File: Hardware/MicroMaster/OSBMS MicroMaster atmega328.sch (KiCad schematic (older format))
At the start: 8 parts

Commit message: changing resistor design
changing resistor design to be cheaper to make and put out a more
manageable amount of heat.
previous design archived
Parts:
- removed U?: PHOTORESISTOR, symbol PHOTORESISTOR
- added Q? (x2): FDS6892A, SO8, symbol FDS6892A
- added R?: 100 ohm, symbol R
- added R?: 4.7k, symbol R
- added U? (x2): optoisolator, symbol optoisolator
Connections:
- net labels added: +3.3V, CLK, CS_N, GND, IRQ, MISO, MOSI, PD-N, RST, RXI, SCK, TXO
- wire segments 0 -> 31
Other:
- moved on the sheet: P?
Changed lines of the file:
@@
 LIBS:contrib
 LIBS:valves
+LIBS:Open source BMS
+LIBS:ata6870n_bms
 LIBS:OSBMS MicroMaster atmega328-cache
 EELAYER 25 0
@@
 L CONN_01X09 P?
 U 1 1 5434A7AE
-P 9450 1150
-F 0 "P?" H 9450 1650 50  0000 C CNN
-F 1 "CONN_01X09" V 9550 1150 50  0000 C CNN
-F 2 "" H 9450 1150 60  0000 C CNN
-F 3 "" H 9450 1150 60  0000 C CNN
-	1    9450 1150
-	0    -1   -1   0
+P 10850 2150
+F 0 "P?" H 10850 2650 50  0000 C CNN
+F 1 "CONN_01X09" V 10950 2150 50  0000 C CNN
+F 2 "" H 10850 2150 60  0000 C CNN
+F 3 "" H 10850 2150 60  0000 C CNN
+	1    10850 2150
+	1    0    0    -1
 $EndComp
 $Comp
 L CONN_01X06 P?
 U 1 1 5434A9A3
-P 10800 2850
-F 0 "P?" H 10800 3200 50  0000 C CNN
-F 1 "CONN_01X06" V 10900 2850 50  0000 C CNN
-F 2 "" H 10800 2850 60  0000 C CNN
-F 3 "" H 10800 2850 60  0000 C CNN
-	1    10800 2850
+P 10850 1100
+F 0 "P?" H 10850 1450 50  0000 C CNN
+F 1 "CONN_01X06" V 10950 1100 50  0000 C CNN
+F 2 "" H 10850 1100 60  0000 C CNN
+F 3 "" H 10850 1100 60  0000 C CNN
+	1    10850 1100
 	1    0    0    -1
 $EndComp
@@
 $EndComp
 $Comp
-L PHOTORESISTOR U?
-U 1 1 5434AFBF
-P 9250 5650
-F 0 "U?" H 9260 5970 70  0000 C CNN
-F 1 "PHOTORESISTOR" H 9260 5330 70  0000 C CNN
-F 2 "" H 9250 5650 60  0000 C CNN
-F 3 "" H 9250 5650 60  0000 C CNN
-	1    9250 5650
-	1    0    0    -1
-$EndComp
+L FDS6892A Q?
+U 1 1 543559EE
+P 8800 2850
+F 0 "Q?" H 8800 2701 40  0000 R CNN
+F 1 "FDS6892A" H 8800 3000 40  0000 R CNN
+F 2 "SO8" H 8670 2952 25  0000 C CIN
+F 3 "" H 8800 2850 60  0000 C CNN
+	1    8800 2850
+	1    0    0    -1
+$EndComp
+$Comp
+L FDS6892A Q?
+U 2 1 54355A39
+P 8800 3500
+F 0 "Q?" H 8800 3351 40  0000 R CNN
+F 1 "FDS6892A" H 8800 3650 40  0000 R CNN
+F 2 "SO8" H 8670 3602 25  0000 C CIN
+F 3 "" H 8800 3500 60  0000 C CNN
+	2    8800 3500
+	1    0    0    -1
+$EndComp
+$Comp
+L +3.3V #PWR?
+U 1 1 54358F9D
+P 10000 2400
+F 0 "#PWR?" H 10000 2360 30  0001 C CNN
+F 1 "+3.3V" H 10000 2510 30  0000 C CNN
+F 2 "" H 10000 2400 60  0000 C CNN
+F 3 "" H 10000 2400 60  0000 C CNN
+	1    10000 2400
+	1    0    0    -1
+$EndComp
+$Comp
+L GND #PWR?
+U 1 1 54358FB1
+P 10550 2650
+F 0 "#PWR?" H 10550 2650 30  0001 C CNN
+F 1 "GND" H 10550 2580 30  0001 C CNN
+F 2 "" H 10550 2650 60  0000 C CNN
+F 3 "" H 10550 2650 60  0000 C CNN
+	1    10550 2650
+	1    0    0    -1
+$EndComp
+Text HLabel 10550 1750 0    60   Input ~ 0
+MISO
+Text HLabel 10550 1850 0    60   Input ~ 0
+MOSI
+Text HLabel 10550 1950 0    60   Input ~ 0
+SCK
+Text HLabel 10550 2050 0    60   Input ~ 0
+CS_N
+Text HLabel 10550 2150 0    60   Input ~ 0
+CLK
+Text HLabel 10550 2250 0    60   Input ~ 0
+IRQ
+Wire Wire Line
+	10550 1750 10650 1750
+Wire Wire Line
+	10550 1850 10650 1850
+Wire Wire Line
+	10550 1950 10650 1950
+Wire Wire Line
+	10550 2050 10650 2050
+Wire Wire Line
+	10550 2150 10650 2150
+Wire Wire Line
+	10550 2250 10650 2250
+Wire Wire Line
+	10650 2550 10550 2550
+Wire Wire Line
+	10550 2550 10550 2650
+Wire Wire Line
+	10650 2450 10000 2450
+Wire Wire Line
+	10000 2450 10000 2400
+Text HLabel 10450 2350 0    60   Input ~ 0
+PD-N
+Text HLabel 10600 1550 0    60   Input ~ 0
+RST
+Text HLabel 8650 1600 0    60   Output ~ 0
+TXO
+Text HLabel 8550 800  0    60   Input ~ 0
+RXI
+Wire Wire Line
+	10650 850  10600 850
+Wire Wire Line
+	10250 950  10650 950
+Connection ~ 10600 950
+Wire Wire Line
+	10550 1350 10650 1350
+Wire Wire Line
+	10350 1250 10650 1250
+Wire Wire Line
+	10350 1150 10650 1150
+Wire Wire Line
+	10600 850  10600 950
+$Comp
+L optoisolator U?
+U 1 1 5435E6BE
+P 9150 1500
+F 0 "U?" H 9150 1700 70  0000 C CNN
+F 1 "optoisolator" H 9160 1180 70  0001 C CNN
+F 2 "" H 9180 1500 60  0000 C CNN
+F 3 "" H 9180 1500 60  0000 C CNN
+	1    9150 1500
+	1    0    0    -1
+$EndComp
+$Comp
+L optoisolator U?
+U 1 1 5435EA84
+P 9150 950
+F 0 "U?" H 9150 1150 70  0000 C CNN
+F 1 "optoisolator" H 9160 630 70  0001 C CNN
+F 2 "" H 9180 950 60  0000 C CNN
+F 3 "" H 9180 950 60  0000 C CNN
+	1    9150 950
+	-1   0    0    -1
+$EndComp
+$Comp
+L R R?
+U 1 1 54360FDA
+P 9950 850
+F 0 "R?" V 10030 850 40  0000 C CNN
+F 1 "100 ohm" V 9957 851 40  0000 C CNN
+F 2 "" V 9880 850 30  0000 C CNN
+F 3 "" H 9950 850 30  0000 C CNN
+	1    9950 850
+	0    1    1    0
+$EndComp
+$Comp
+L R R?
+U 1 1 54361025
+P 9950 1250
+F 0 "R?" V 10030 1250 40  0000 C CNN
+F 1 "4.7k" V 9957 1251 40  0000 C CNN
+F 2 "" V 9880 1250 30  0000 C CNN
+F 3 "" H 9950 1250 30  0000 C CNN
+	1    9950 1250
+	0    1    1    0
+$EndComp
+Wire Wire Line
+	9600 850  9700 850
+Wire Wire Line
+	10200 850  10350 850
+Wire Wire Line
+	10350 850  10350 1150
+Wire Wire Line
+	9600 1050 10250 1050
+Wire Wire Line
+	10250 950  10250 1250
+Wire Wire Line
+	10250 1250 10200 1250
+Connection ~ 10250 1050
+Wire Wire Line
+	9700 1250 9650 1250
+Wire Wire Line
+	9650 1250 9650 1600
+Wire Wire Line
+	9650 1600 9600 1600
+Wire Wire Line
+	9600 1400 9600 1100
+Wire Wire Line
+	9600 1100 10550 1100
+Wire Wire Line
+	10550 1100 10550 1050
+Wire Wire Line
+	10550 1050 10650 1050
+Wire Wire Line
+	10350 1250 10350 1400
+Wire Wire Line
+	10350 1400 9650 1400
+Connection ~ 9650 1400
 $EndSCHEMATC

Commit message: Completed preliminary test program
created a test program that reads cell voltages out to serial (raw adc
values, not scaled voltages). this sketch also contains a lot of
partially working functions for future functionality.

also updated was the atmega328 based master board. - which is not quite
complete
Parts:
- removed Q? (x2): FDS6892A, SO8, symbol FDS6892A
- added C?: Csmall, symbol Csmall
- added C? (x3): 100NF, symbol Csmall
- added P?: CONN_01X03, symbol CONN_01X03
- added R?: 3k, Resistors_SMD:R_0603, symbol R
- added R?: 100 ohm, Resistors_SMD:R_0603, symbol R
- added R?: 10K, Resistors_SMD:R_0603, symbol R
- added R?: 4.7K, Resistors_SMD:R_0603, symbol R
- R?: footprint (none) -> Resistors_SMD:R_0603
- R?: value 4.7k -> 3k; footprint (none) -> Resistors_SMD:R_0603
- XTAL?: renamed from X?; value CRYSTAL_SMD -> 8mhz resonator
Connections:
- net labels added: 1WireComm, A0, A1, A2, A3, A6, A7, C_Sense1, C_Sense2, D10*, D3*, D4, D5*, D6*, D7, D8, D9*, Int0/2, MOSI/11*, RESET, RXD, S-GND, S-RST, S-RXI, S-TXO, S-VCC, SCK/13, SCL/A5, SDA/A4, TXD
- net labels removed: MOSI, RST, RXI, SCK, TXO
- wire segments 31 -> 120
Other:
- note added: "* = pwm capable pin"
- note added: "1 wire"
- note added: "Current sense"
- note added: "Serial / programming"
- note added: "programming connector"
- note added: "to balance boards"
- moved on the sheet: IC?, P?, R?, XTAL?

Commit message: Fixed test code and schematic
Fixed a problem in the code that caused it to hang. spi now appears to
be working porperly with a logic analyzer.  I also finished up some
stuff with the micromaster schematic. It is now ready to be laied out on
a pcb
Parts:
- added C?: 33uF PolC, Capacitors_Tantalum_SMD:TantalC_SizeA_EIA-3216_Reflow, symbol PolC
- added C?: 100nF, Capacitors_SMD:C_0603, symbol Cap
- added C? (x2): C, symbol C
- added C?: CP1, symbol CP1
- added D?: 3.3v TVS, symbol TVS
- added P? (x2): CONN_01X04, symbol CONN_01X04
- added P?: CONN_01X02, symbol CONN_01X02
- added Q? (x2): FDS6892A, SO8, symbol FDS6892A
- added Q?: BSS138, SOT-23, symbol BSS138
- added R? (x3): 10K, Resistors_SMD:R_0603, symbol R
- added R?: 5k ohm, Resistors_SMD:R_0603, symbol R
- added R?: 50k ohm, Resistors_SMD:R_0603, symbol R
- P?: footprint (none) -> Pin_Headers:Pin_Header_Straight_1x06
- P?: footprint (none) -> Pin_Headers:Pin_Header_Straight_2x03
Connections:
- net labels added: +12V
- net labels removed: CLK, PD-N
- wire segments 120 -> 185
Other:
- note added: "& controller voltage sense"
- note added: "12/24v aux \npower in"
- note added: "Auxilary power outputs\nFor contactor/ETC"
- note added: "Max 20ma draw on 3.3v"
- note added: "precharge relay \n"
- moved on the sheet: C?, IC?, P?, R?, XTAL?

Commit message: Actually fixed code
The last commit had a mistake and this commit actually fixes the program
as well as advancing slightly on the micromaster design
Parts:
- removed C?: Csmall, symbol Csmall
- removed C?: 33uF PolC, Capacitors_Tantalum_SMD:TantalC_SizeA_EIA-3216_Reflow, symbol PolC
- removed C?: 100nF, Capacitors_SMD:C_0603, symbol Cap
- removed C? (x2): C, symbol C
- removed R? (x2): 100 ohm, Resistors_SMD:R_0603, symbol R
- removed R? (x2): 3k, Resistors_SMD:R_0603, symbol R
- removed U? (x2): optoisolator, symbol optoisolator
- added C10: 100nF, Capacitors_SMD:C_0603, symbol Cap
- added C2, C6, C7, C8: 100NF, Capacitors_SMD:C_0603, symbol Csmall
- added C9: 33uF PolC, Capacitors_Tantalum_SMD:TantalC_SizeA_EIA-3216_Reflow, symbol PolC
- added P8: CONN_01X04, Pin_Headers:Pin_Header_Straight_1x04, symbol CONN_01X04
- added P9: CONN_01X06, Connectors_Molex:Connector_Molex_PicoBlade_53261-0671, symbol CONN_01X06
- added R2, R3: 10K, Resistors_SMD:R_0603, symbol R
- C1, C3, C4: renamed from C?; footprint (none) -> Capacitors_SMD:C_0603
- C5: renamed from C?; footprint (none) -> Capacitors_SMD:c_elec_8x10
- D1: renamed from D?; footprint (none) -> SMD_Packages:DO-214-AC_SMA
- IC1: renamed from IC?; footprint TQFP32 -> SMD_Packages:TQFP-32
- P10: renamed from P?; footprint (none) -> Pin_Headers:Pin_Header_Straight_1x04
- P11: renamed from P?; footprint (none) -> Connect:bornier4
- P3, P4, P6: renamed from P?; footprint (none) -> Pin_Headers:Pin_Header_Straight_1x03
- P7: renamed from P?; footprint (none) -> Connect:bornier2
- Q1: renamed from Q?; footprint SO8 -> SMD_Packages:SOIC-8-W
- gave numbers to parts that had none: 12
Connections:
- wire segments 185 -> 187
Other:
- note added: "Current Sense\n Inputs"
- note added: "Decoupling caps"
- note added: "I2C Bus"
- note added: "Other IO"
- note added: "Resistors that are shown in datasheet \nbut never mentioned in text?"
- note added: "Serial connector"
- note added: "ToDo:\n- Clean up schematic so it's somewhat readable\n-check the validity of resistors on spi bus\n- create footpront for ceramic resonator CSTCE8M"
- note removed: "Current sense"
- note removed: "Serial / programming"
- moved on the sheet: C1, C3, C4, P2, P3, P4, P5, R1

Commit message: touched up balancer board and reorganised
touched up balancer board so that it is ready for production,
reorganised a bunch of files and added proper revision labels, and made
good progress on the micromaster board. the schematic is complete, the
board is layed out, some traces still need to be run though.
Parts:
- removed P11: CONN_01X04, Connect:bornier4, symbol CONN_01X04
- removed P6: CONN_01X03, Pin_Headers:Pin_Header_Straight_1x03, symbol CONN_01X03
- removed P7: CONN_01X02, Connect:bornier2, symbol CONN_01X02
- removed P8: CONN_01X04, Pin_Headers:Pin_Header_Straight_1x04, symbol CONN_01X04
- removed P9: CONN_01X06, Connectors_Molex:Connector_Molex_PicoBlade_53261-0671, symbol CONN_01X06
- removed R4: 4.7K, Resistors_SMD:R_0603, symbol R
- removed XTAL1: 8mhz resonator, symbol CRYSTAL_SMD
- added P6: CONN_01X10, Pin_Headers:Pin_Header_Straight_2x05, symbol CONN_01X10
- added P7: CONN_01X06, Connect:bornier6, symbol CONN_01X06
- added XTAL1: 8mhz resonator, SparkFun-FreqCtrl.lbr:RESONATOR-SMD, symbol CRYSTAL_SMD_MURATA
- D1: footprint SMD_Packages:DO-214-AC_SMA -> Diodes_SMD:Diode-MiniMELF_Standard
- P5: footprint (none) -> MyCustomParts:Connector_SMD_GH_SIDECONN_1X9_1.25MM_45515711ND
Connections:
- net +12V: now also P7.1 (P1), P7.3 (P3), P7.5 (P5)
- net +3.3V: now also P2.5 (P5), P6.2 (P2); no longer P2.2 (P2)
- net A0: now also C4.2, P4.1 (P1); no longer C7.2, R5.1, R6.2
- net A1: now also C3.2, P3.1 (P1); no longer C8.2, D1.1, P10.3 (P3)
- net A2: now also P6.3 (P3); no longer C3.2, P3.1 (P1)
- net A3: now also P6.4 (P4); no longer C4.2, P4.1 (P1)
- net A6: now also C8.2, D1.1, P10.3 (P3)
- net A7: now also C7.2, R5.1, R6.2
- net D10*: now also P6.10 (P10)
- net D3*: now also P6.7 (P7)
- net D4: now also P6.8 (P8); no longer Q2.1 (G), R8.2
- net D7: now also Q2.1 (G), R8.2
- net D9*: now also P6.9 (P9)
- net GND: now also P2.1 (P1), P6.1 (P1), P7.2 (P2), XTAL1.2; no longer P2.6 (P6)
- net MISO: now also P2.6 (P6); no longer P2.1 (P1)
- net RESET: now also P2.2 (P2); no longer P2.5 (P5)
- net SCK/13: now also P2.4 (P4); no longer P2.3 (P3)
- net SCL/A5: now also P6.6 (P6)
- net SDA/A4: now also P6.5 (P5)
- net at IC1.7 ((PCINT6/XTAL1/TOSC1)PB6): now also XTAL1.3
- net at IC1.8 ((PCINT7/XTAL2/TOSC2)PB7): now also XTAL1.1
- net at Q1.7 (D), Q1.8 (D): now also P7.4 (P4)
- net at Q1.5 (D), Q1.6 (D): now also P7.6 (P6)
- net MOSI/11* renamed MOSI
- net MOSI: now also P2.3 (P3); no longer P2.4 (P4)
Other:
- note removed: "1 wire"
- note removed: "I2C Bus"
- moved on the sheet: C5, C7, C8, D1, P10, Q1A, Q1B, Q2, R5, R6, R7, R8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

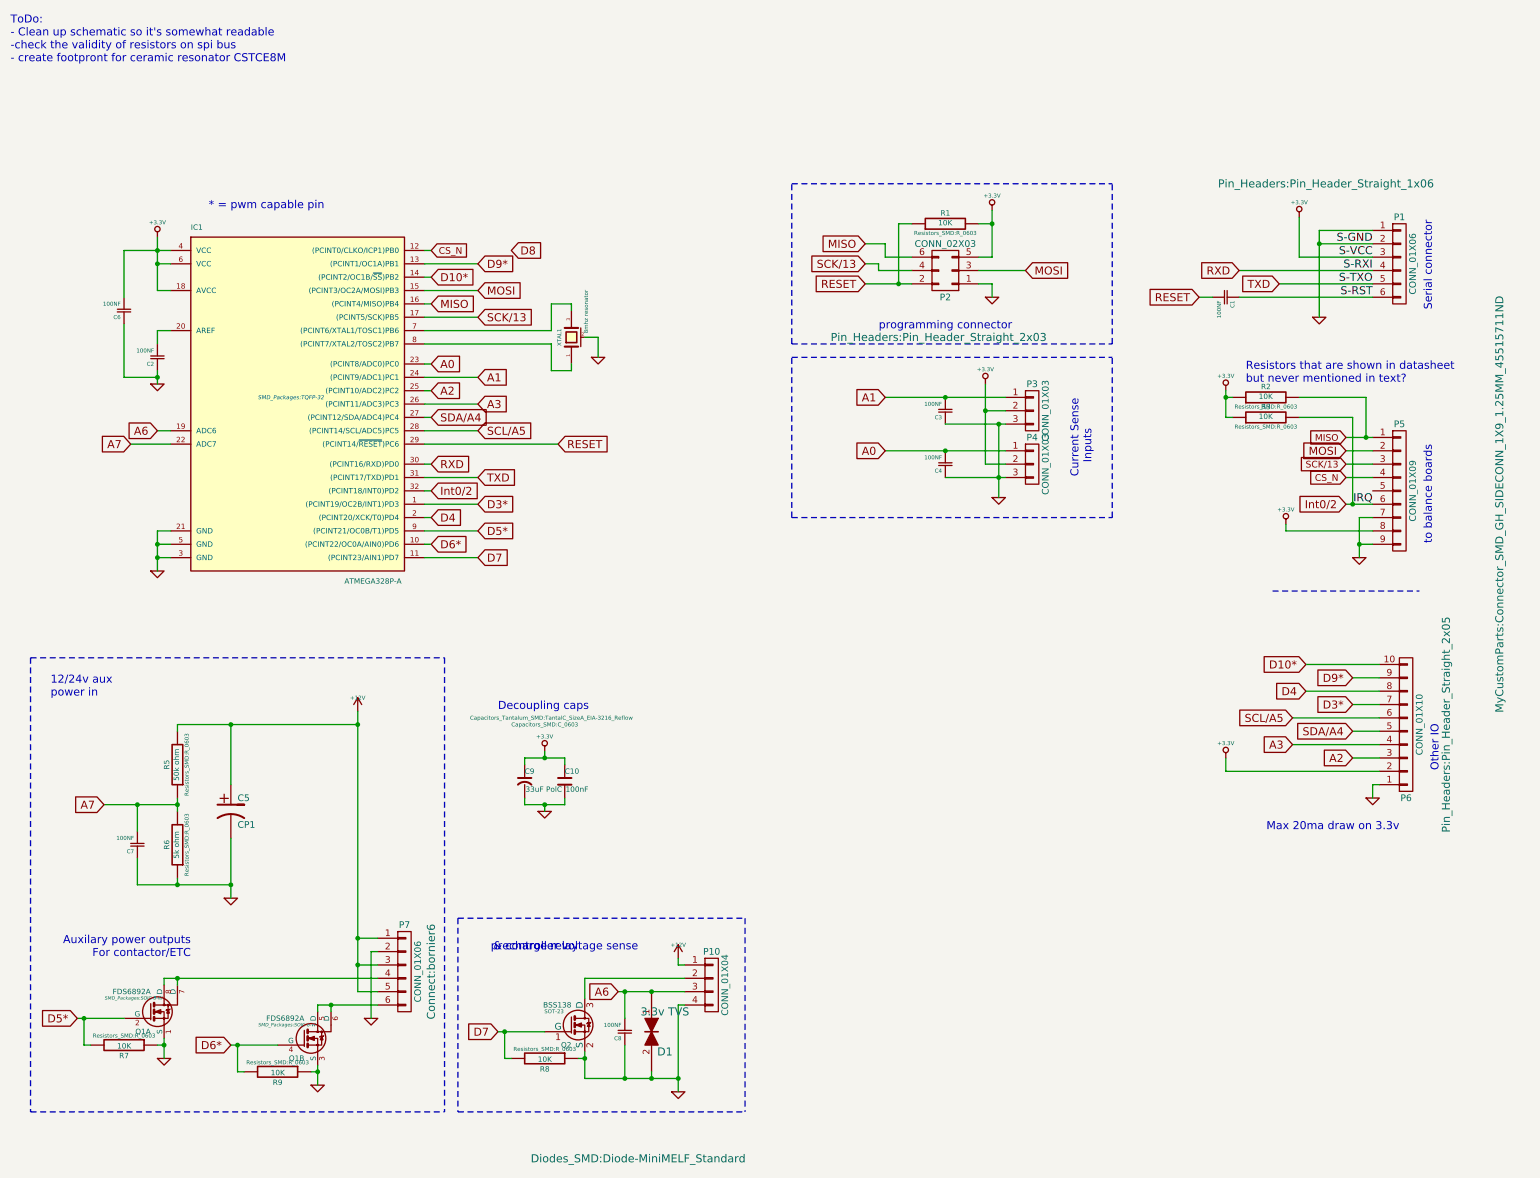
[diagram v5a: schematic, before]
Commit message: Rev1 READY!
All the boards have been completed and arre ready for prototype
production. docunentation has been updated and the docs folder now
contains schematic pdf's, rendered pictures, and completed bill of
materials for both boarrds.

The software also recieved an update that corrected a datatype error and
shouuld make it testing ready.
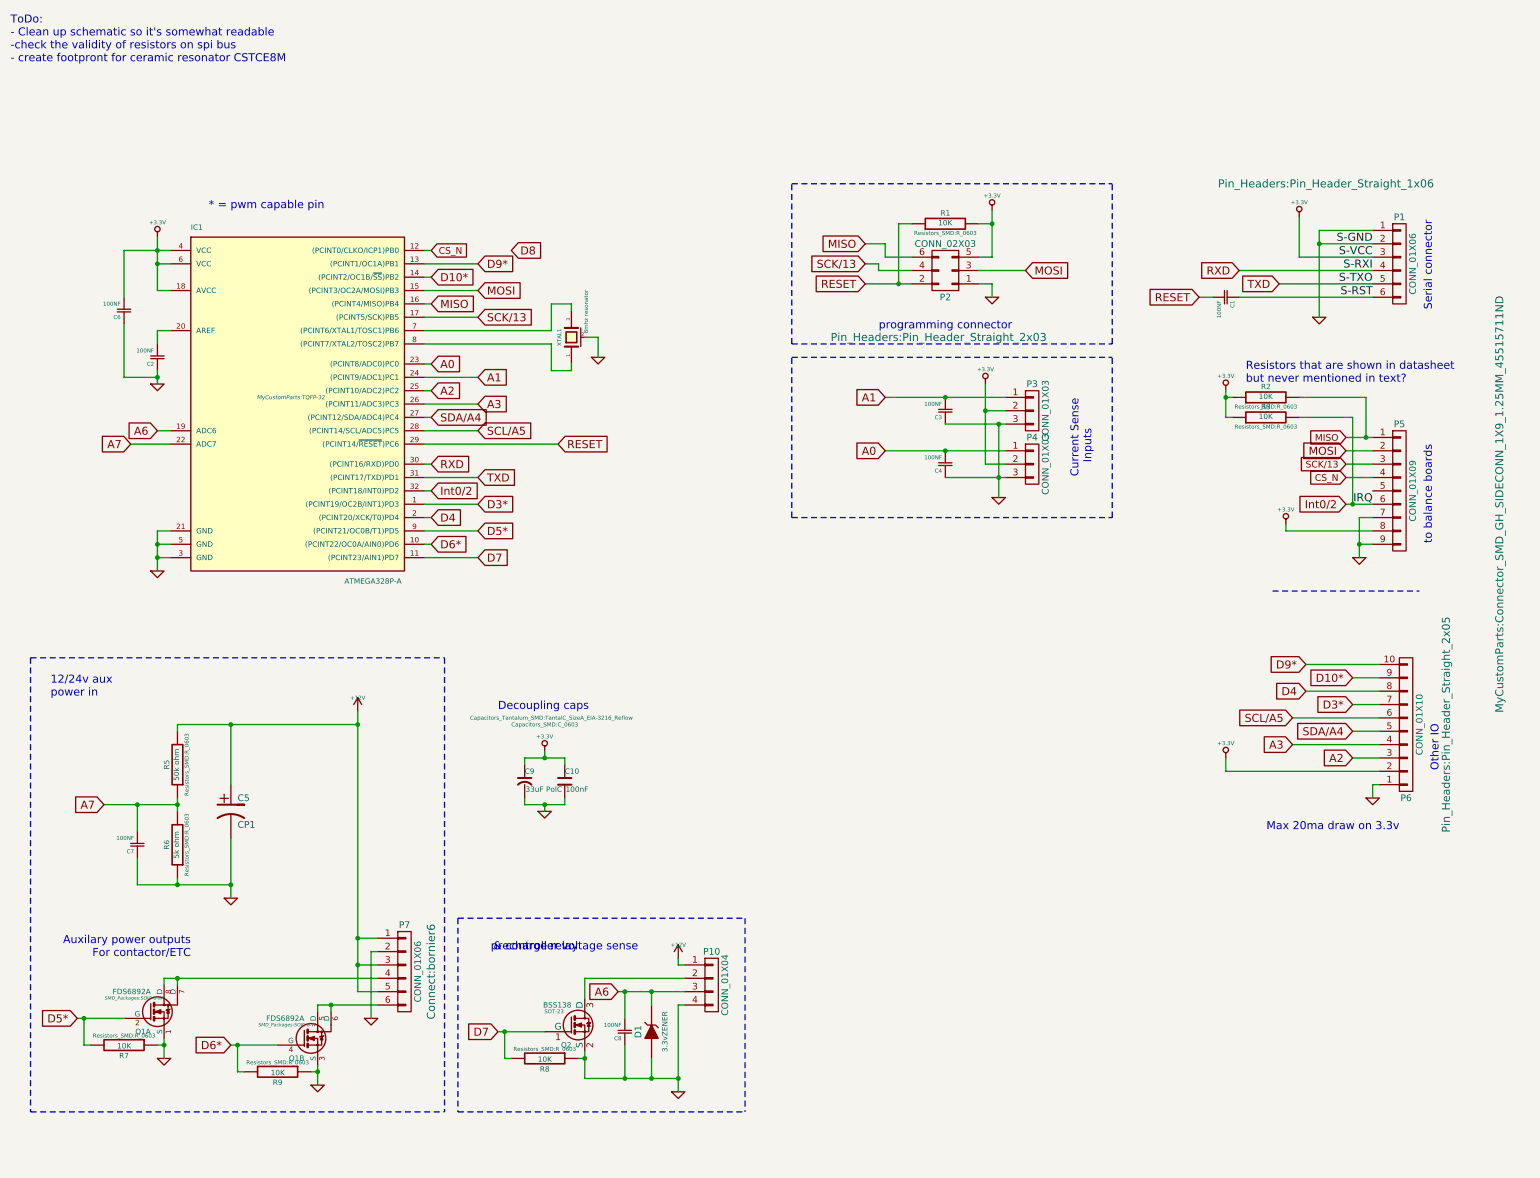
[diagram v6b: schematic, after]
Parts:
- removed D1: 3.3v TVS, Diodes_SMD:Diode-MiniMELF_Standard, symbol TVS
- added D1: 3.3vZENER, SMD_Packages:SOD-523, symbol ZENER
- IC1: footprint SMD_Packages:TQFP-32 -> MyCustomParts:TQFP-32
- XTAL1: footprint SparkFun-FreqCtrl.lbr:RESONATOR-SMD -> MyCustomParts:RESONATOR-SMD-mutera
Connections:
- net A6: now also D1.2 (K)
- net D10*: now also P6.9 (P9); no longer P6.10 (P10)
- net D9*: now also P6.10 (P10); no longer P6.9 (P9)
- net GND: now also D1.1 (A)
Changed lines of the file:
@@
 F 0 "IC1" H 1800 3600 40  0000 L BNN
 F 1 "ATMEGA328P-A" H 2950 950 40  0000 L BNN
-F 2 "SMD_Packages:TQFP-32" H 2550 2350 30  0000 C CIN
+F 2 "MyCustomParts:TQFP-32" H 2550 2350 30  0000 C CIN
 F 3 "" H 2550 2350 60  0000 C CNN
 	1    2550 2350
@@
 $EndComp
 $Comp
-L TVS D1
-U 1 1 5464D2CC
-P 5250 7100
-F 0 "D1" V 5400 7200 60  0000 C CNN
-F 1 "3.3v TVS" V 5100 7200 60  0000 C CNN
-F 2 "Diodes_SMD:Diode-MiniMELF_Standard" V 6200 7000 60  0000 C CNN
-F 3 "" H 5250 7100 60  0000 C CNN
-	1    5250 7100
-	0    1    1    0
-$EndComp
-$Comp
 L GND #PWR019
 U 1 1 5464D2EC
@@
 Text GLabel 10500 4650 0    60   Input ~ 0
 D3*
+Text GLabel 10150 4350 0    60   Input ~ 0
+D9*
 Text GLabel 10500 4450 0    60   Input ~ 0
-D9*
-Text GLabel 10150 4350 0    60   Input ~ 0
 D10*
 $Comp
@@
 	4750 7450 5450 7450
 Wire Wire Line
-	5250 7450 5250 7400
+	5250 7300 5250 7450
 Wire Wire Line
 	5450 6900 5450 7550
@@
 F 0 "XTAL1" H 4650 1990 30  0000 C CNN
 F 1 "8mhz resonator" H 4680 1790 30  0000 L CNN
-F 2 "SparkFun-FreqCtrl.lbr:RESONATOR-SMD" H 4650 1900 60  0001 C CNN
+F 2 "MyCustomParts:RESONATOR-SMD-mutera" H 4650 1900 60  0001 C CNN
 F 3 "" H 4650 1900 60  0000 C CNN
 	1    4650 1900
@@
 Text GLabel 10450 2750 0    60   Input ~ 0
 MOSI
+$Comp
+L ZENER D1
+U 1 1 54694E07
+P 5250 7100
+F 0 "D1" H 5250 7200 50  0000 C CNN
+F 1 "3.3vZENER" H 5250 7000 40  0000 C CNN
+F 2 "SMD_Packages:SOD-523" V 4800 7600 60  0001 C CNN
+F 3 "" H 5250 7100 60  0000 C CNN
+	1    5250 7100
+	0    -1   -1   0
+$EndComp
+Wire Wire Line
+	5250 6800 5250 6900
 $EndSCHEMATC
